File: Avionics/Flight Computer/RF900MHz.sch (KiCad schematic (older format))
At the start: 25 parts, among them J1 CONN_COAXIAL, U1 CC1310F128RGZR, U2 CC1190RGVR

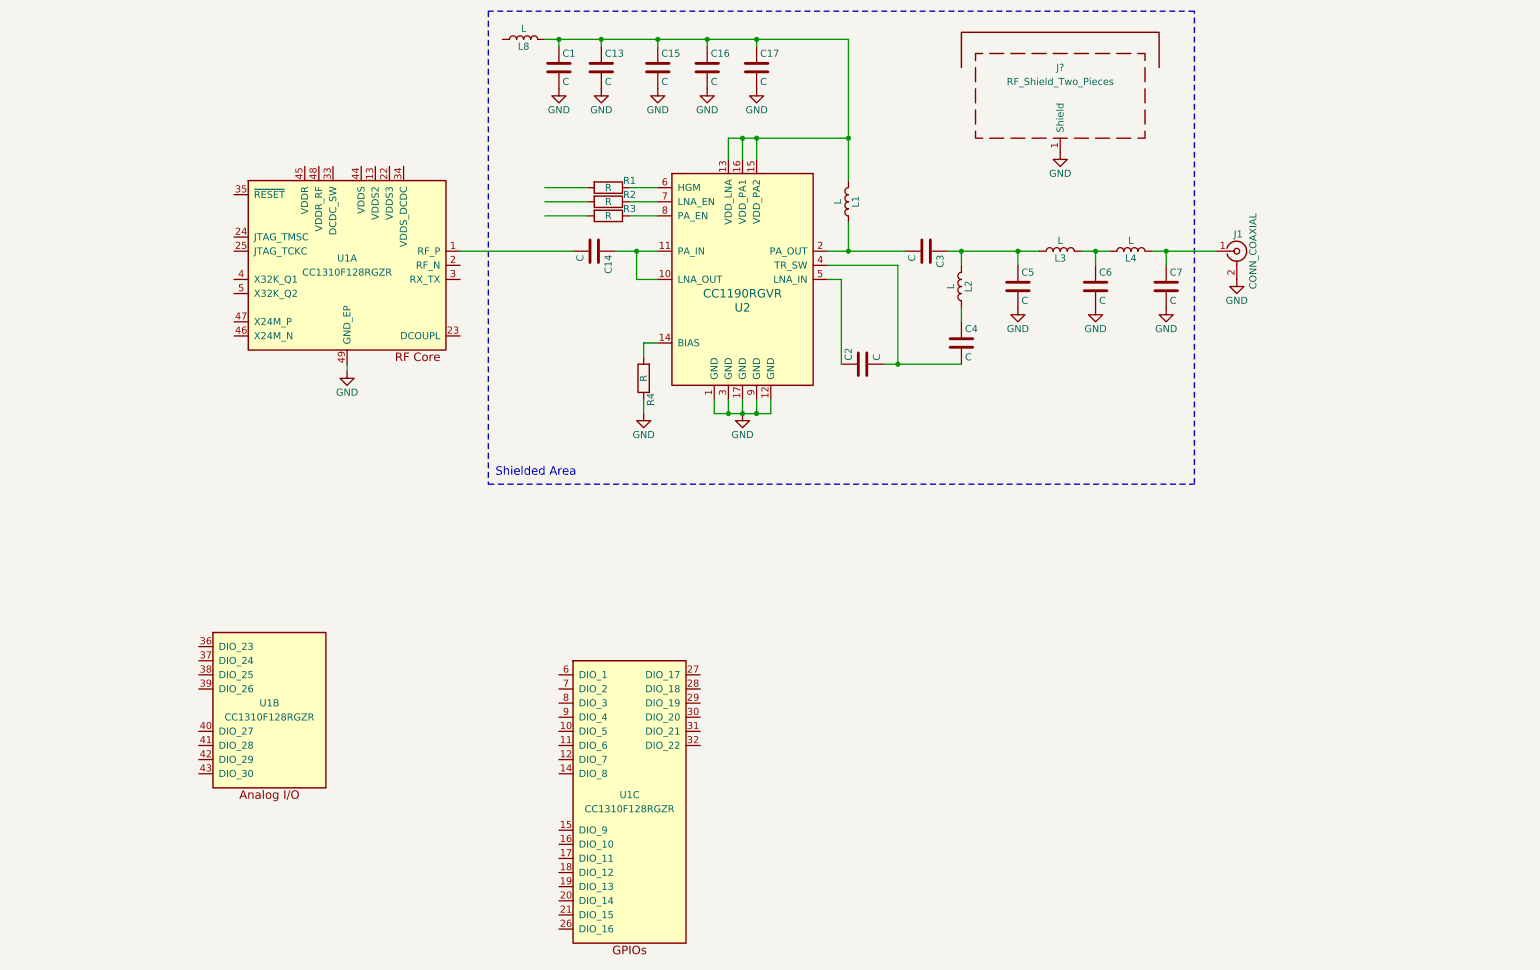
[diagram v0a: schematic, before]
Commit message: Added more RF passives and placement of RF front ends
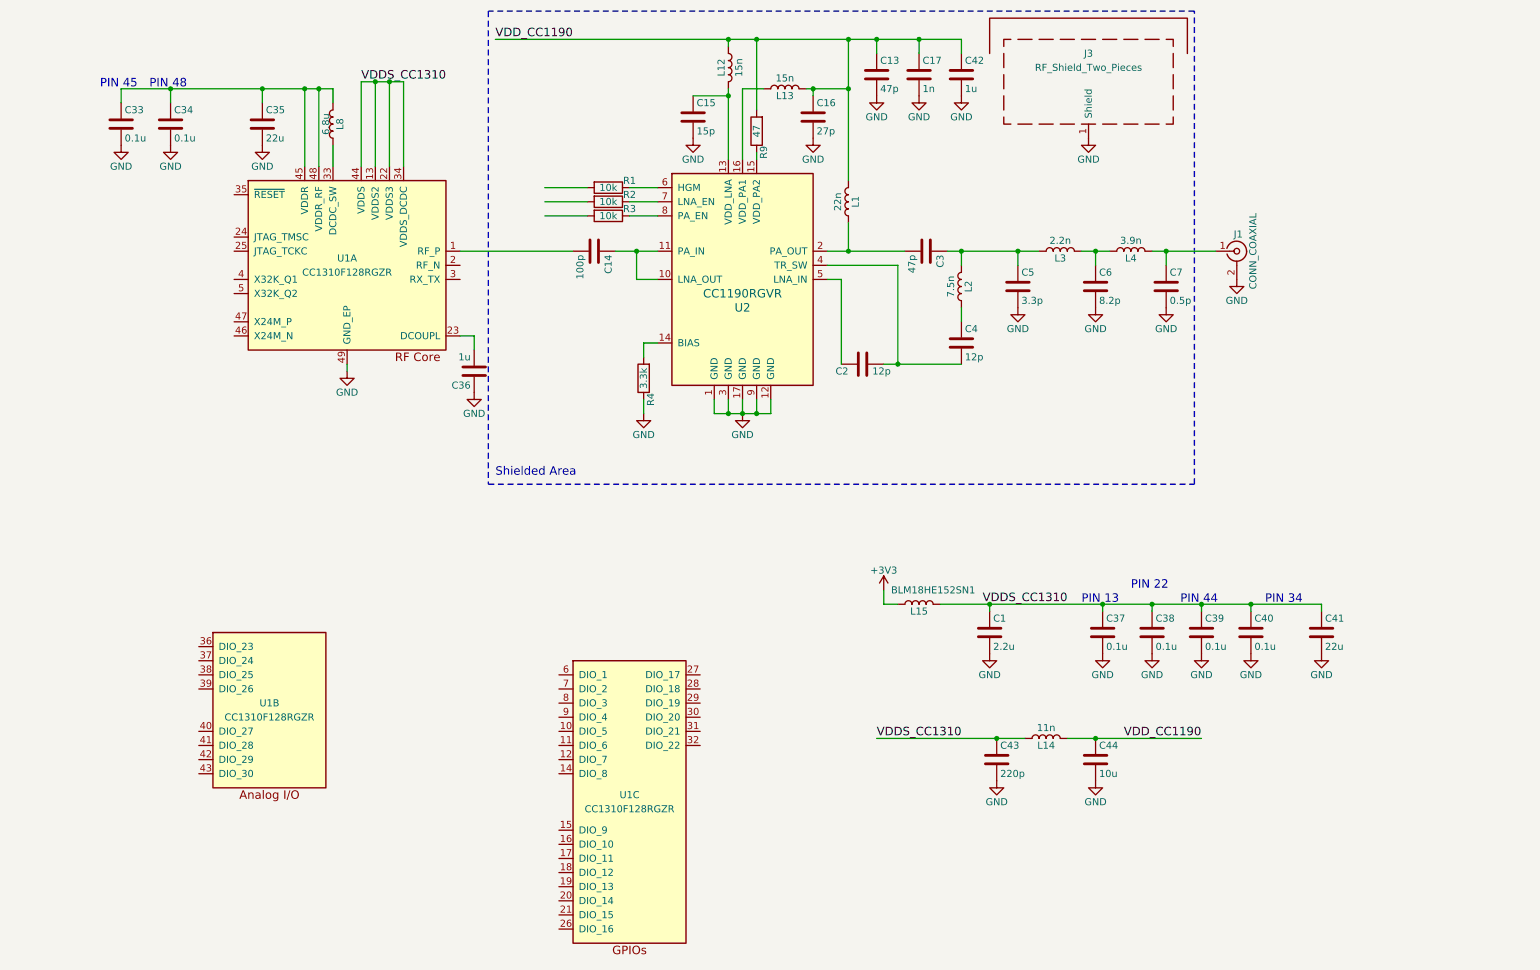
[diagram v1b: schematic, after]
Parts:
- added C33, C34, C37, C38, C39, C40: 0.1u, Capacitors_SMD:C_0402, symbol C
- added C35, C41: 22u, Capacitors_SMD:C_0603, symbol C
- added C36, C42: 1u, Capacitors_SMD:C_0402, symbol C
- added C43: 220p, Capacitors_SMD:C_0402, symbol C
- added C44: 10u, Capacitors_SMD:C_0603, symbol C
- added L12, L13: 15n, Inductors_SMD:L_0402, symbol L
- added L14: 11n, Inductors_SMD:L_0603, symbol L
- added L8: 6.8u, Inductors_SMD:L_0402, symbol L
- added R9: 47, Resistors_SMD:R_0402, symbol R
- C1: value C -> 2.2u
- C13, C3: value C -> 47p
- C14: value C -> 100p
- C15: value C -> 15p
- C16: value C -> 27p
- C17: value C -> 1n
- C2, C4: value C -> 12p
- C5: value C -> 3.3p
- C6: value C -> 8.2p
- C7: value C -> 0.5p
- L1: value L -> 22n; footprint Inductors_SMD:L_0402 -> Inductors_SMD:L_0603
- L15: renamed from L8; value L -> BLM18HE152SN1
- L2: value L -> 7.5n
- L3: value L -> 2.2n
- L4: value L -> 3.9n
- R1, R2, R3: value R -> 10k; footprint (none) -> Resistors_SMD:R_0402
- R4: value R -> 3.3k; footprint (none) -> Resistors_SMD:R_0402
- gave numbers to parts that had none: 1
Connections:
- net labels added: +3V3, VDDS_CC1310, VDD_CC1190
- wire segments 46 -> 75
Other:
- note added: "PIN 13"
- note added: "PIN 22"
- note added: "PIN 34"
- note added: "PIN 44"
- note added: "PIN 45"
- note added: "PIN 48"
- moved on the sheet: C1, C13, J3, L15

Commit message: Lots of power tree and layout work
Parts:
- J3: value RF_Shield_Two_Pieces -> BMI-S-202-F
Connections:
- net labels added: +3.3V
- net labels removed: +3V3
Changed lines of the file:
@@
 LIBS:graphic
 LIBS:power
+LIBS:interface
+LIBS:linear
+LIBS:74xgxx
+LIBS:74xx
+LIBS:ac-dc
+LIBS:actel
+LIBS:adc-dac
+LIBS:allegro
+LIBS:Altera
+LIBS:analog_devices
+LIBS:analog_switches
+LIBS:Power_Management
+LIBS:powerint
 LIBS:Flight Computer-cache
-EELAYER 25 0
+EELAYER 26 0
 EELAYER END
 $Descr A4 11693 8268
@@
 $EndComp
 $Comp
-L GND #PWR28
+L GND #PWR05
 U 1 1 58AA1A95
 P 9000 2500
-F 0 "#PWR28" H 9000 2250 50  0001 C CNN
+F 0 "#PWR05" H 9000 2250 50  0001 C CNN
 F 1 "GND" H 9000 2350 50  0000 C CNN
 F 2 "" H 9000 2500 50  0001 C CNN
@@
 $EndComp
 $Comp
-L GND #PWR26
+L GND #PWR06
 U 1 1 58AA3683
 P 8500 2700
-F 0 "#PWR26" H 8500 2450 50  0001 C CNN
+F 0 "#PWR06" H 8500 2450 50  0001 C CNN
 F 1 "GND" H 8500 2550 50  0000 C CNN
 F 2 "" H 8500 2700 50  0001 C CNN
@@
 $EndComp
 $Comp
-L GND #PWR22
+L GND #PWR07
 U 1 1 58AA36BB
 P 8000 2700
-F 0 "#PWR22" H 8000 2450 50  0001 C CNN
+F 0 "#PWR07" H 8000 2450 50  0001 C CNN
 F 1 "GND" H 8000 2550 50  0000 C CNN
 F 2 "" H 8000 2700 50  0001 C CNN
@@
 $EndComp
 $Comp
-L GND #PWR20
+L GND #PWR08
 U 1 1 58AA36F3
 P 7450 2700
-F 0 "#PWR20" H 7450 2450 50  0001 C CNN
+F 0 "#PWR08" H 7450 2450 50  0001 C CNN
 F 1 "GND" H 7450 2550 50  0000 C CNN
 F 2 "" H 7450 2700 50  0001 C CNN
@@
 $EndComp
 $Comp
-L GND #PWR12
+L GND #PWR09
 U 1 1 58AA409E
 P 5500 3450
-F 0 "#PWR12" H 5500 3200 50  0001 C CNN
+F 0 "#PWR09" H 5500 3200 50  0001 C CNN
 F 1 "GND" H 5500 3300 50  0000 C CNN
 F 2 "" H 5500 3450 50  0001 C CNN
@@
 $EndComp
 $Comp
-L GND #PWR8
+L GND #PWR010
 U 1 1 58AA431F
 P 2700 3150
-F 0 "#PWR8" H 2700 2900 50  0001 C CNN
+F 0 "#PWR010" H 2700 2900 50  0001 C CNN
 F 1 "GND" H 2700 3000 50  0000 C CNN
 F 2 "" H 2700 3150 50  0001 C CNN
@@
 $EndComp
 $Comp
-L GND #PWR18
+L GND #PWR011
 U 1 1 58AABD29
 P 7250 5150
-F 0 "#PWR18" H 7250 4900 50  0001 C CNN
+F 0 "#PWR011" H 7250 4900 50  0001 C CNN
 F 1 "GND" H 7250 5000 50  0000 C CNN
 F 2 "" H 7250 5150 50  0001 C CNN
@@
 $EndComp
 $Comp
-L GND #PWR11
+L GND #PWR012
 U 1 1 58AAF7AF
 P 5150 1500
-F 0 "#PWR11" H 5150 1250 50  0001 C CNN
+F 0 "#PWR012" H 5150 1250 50  0001 C CNN
 F 1 "GND" H 5150 1350 50  0000 C CNN
 F 2 "" H 5150 1500 50  0001 C CNN
@@
 $EndComp
 $Comp
-L GND #PWR10
+L GND #PWR013
 U 1 1 58AB0BB7
 P 4800 3450
-F 0 "#PWR10" H 4800 3200 50  0001 C CNN
+F 0 "#PWR013" H 4800 3200 50  0001 C CNN
 F 1 "GND" H 4800 3300 50  0000 C CNN
 F 2 "" H 4800 3450 50  0001 C CNN
@@
 $EndComp
 $Comp
-L GND #PWR21
+L GND #PWR014
 U 1 1 58AB2D32
 P 7950 1500
-F 0 "#PWR21" H 7950 1250 50  0001 C CNN
+F 0 "#PWR014" H 7950 1250 50  0001 C CNN
 F 1 "GND" H 7950 1350 50  0000 C CNN
 F 2 "" H 7950 1500 50  0001 C CNN
@@
 P 7950 1100
 F 0 "J3" H 7950 1300 50  0000 C CNN
-F 1 "RF_Shield_Two_Pieces" H 7950 1200 50  0000 C CNN
+F 1 "BMI-S-202-F" H 7950 1200 50  0000 C CNN
 F 2 "Shielding_Cabinets:Laird_Technologies_BMI-S-202-F_16.50x16.50mm" H 7950 1000 50  0001 C CNN
 F 3 "" H 7950 1000 50  0001 C CNN
@@
 Text Label 7200 4800 0    60   ~ 0
 VDDS_CC1310
-$Comp
-L +3V3 #PWR15
-U 1 1 58AE2EAF
-P 6500 4700
-F 0 "#PWR15" H 6500 4550 50  0001 C CNN
-F 1 "+3V3" H 6500 4840 50  0000 C CNN
-F 2 "" H 6500 4700 50  0001 C CNN
-F 3 "" H 6500 4700 50  0001 C CNN
-	1    6500 4700
-	1    0    0    -1
-$EndComp
 $Comp
 L C C36
@@
 $EndComp
 $Comp
-L GND #PWR9
+L GND #PWR015
 U 1 1 58AE74D7
 P 3600 3300
-F 0 "#PWR9" H 3600 3050 50  0001 C CNN
+F 0 "#PWR015" H 3600 3050 50  0001 C CNN
 F 1 "GND" H 3600 3150 50  0000 C CNN
 F 2 "" H 3600 3300 50  0001 C CNN
@@
 $EndComp
 $Comp
-L GND #PWR24
+L GND #PWR016
 U 1 1 58AF2937
 P 8050 5150
-F 0 "#PWR24" H 8050 4900 50  0001 C CNN
+F 0 "#PWR016" H 8050 4900 50  0001 C CNN
 F 1 "GND" H 8050 5000 50  0000 C CNN
 F 2 "" H 8050 5150 50  0001 C CNN
@@
 $EndComp
 $Comp
-L GND #PWR25
+L GND #PWR017
 U 1 1 58AF2A67
 P 8400 5150
-F 0 "#PWR25" H 8400 4900 50  0001 C CNN
+F 0 "#PWR017" H 8400 4900 50  0001 C CNN
 F 1 "GND" H 8400 5000 50  0000 C CNN
 F 2 "" H 8400 5150 50  0001 C CNN
@@
 $EndComp
 $Comp
-L GND #PWR27
+L GND #PWR018
 U 1 1 58AF2BB0
 P 8750 5150
-F 0 "#PWR27" H 8750 4900 50  0001 C CNN
+F 0 "#PWR018" H 8750 4900 50  0001 C CNN
 F 1 "GND" H 8750 5000 50  0000 C CNN
 F 2 "" H 8750 5150 50  0001 C CNN
@@
 $EndComp
 $Comp
-L GND #PWR29
+L GND #PWR019
 U 1 1 58AF2C21
 P 9100 5150
-F 0 "#PWR29" H 9100 4900 50  0001 C CNN
+F 0 "#PWR019" H 9100 4900 50  0001 C CNN
 F 1 "GND" H 9100 5000 50  0000 C CNN
 F 2 "" H 9100 5150 50  0001 C CNN
@@
 	9600 4800 9600 4850
 $Comp
-L GND #PWR30
+L GND #PWR020
 U 1 1 58AF39C7
 P 9600 5150
-F 0 "#PWR30" H 9600 4900 50  0001 C CNN
+F 0 "#PWR020" H 9600 4900 50  0001 C CNN
 F 1 "GND" H 9600 5000 50  0000 C CNN
 F 2 "" H 9600 5150 50  0001 C CNN
@@
 Connection ~ 2500 1150
 $Comp
-L GND #PWR7
+L GND #PWR021
 U 1 1 58AF55B9
 P 2100 1550
-F 0 "#PWR7" H 2100 1300 50  0001 C CNN
+F 0 "#PWR021" H 2100 1300 50  0001 C CNN
 F 1 "GND" H 2100 1400 50  0000 C CNN
 F 2 "" H 2100 1550 50  0001 C CNN
@@
 Connection ~ 1450 1150
 $Comp
-L GND #PWR6
+L GND #PWR022
 U 1 1 58AF6EFE
 P 1450 1550
-F 0 "#PWR6" H 1450 1300 50  0001 C CNN
+F 0 "#PWR022" H 1450 1300 50  0001 C CNN
 F 1 "GND" H 1450 1400 50  0000 C CNN
 F 2 "" H 1450 1550 50  0001 C CNN
@@
 $EndComp
 $Comp
-L GND #PWR5
+L GND #PWR023
 U 1 1 58AF6F78
 P 1100 1550
-F 0 "#PWR5" H 1100 1300 50  0001 C CNN
+F 0 "#PWR023" H 1100 1300 50  0001 C CNN
 F 1 "GND" H 1100 1400 50  0000 C CNN
 F 2 "" H 1100 1550 50  0001 C CNN
@@
 $EndComp
 $Comp
-L GND #PWR14
+L GND #PWR024
 U 1 1 58AF9836
 P 6450 1200
-F 0 "#PWR14" H 6450 950 50  0001 C CNN
+F 0 "#PWR024" H 6450 950 50  0001 C CNN
 F 1 "GND" H 6450 1050 50  0000 C CNN
 F 2 "" H 6450 1200 50  0001 C CNN
@@
 $EndComp
 $Comp
-L GND #PWR16
+L GND #PWR025
 U 1 1 58AF99F1
 P 6750 1200
-F 0 "#PWR16" H 6750 950 50  0001 C CNN
+F 0 "#PWR025" H 6750 950 50  0001 C CNN
 F 1 "GND" H 6750 1050 50  0000 C CNN
 F 2 "" H 6750 1200 50  0001 C CNN
@@
 $EndComp
 $Comp
-L GND #PWR17
+L GND #PWR026
 U 1 1 58AF9A68
 P 7050 1200
-F 0 "#PWR17" H 7050 950 50  0001 C CNN
+F 0 "#PWR026" H 7050 950 50  0001 C CNN
 F 1 "GND" H 7050 1050 50  0000 C CNN
 F 2 "" H 7050 1200 50  0001 C CNN
@@
 Connection ~ 6000 1150
 $Comp
-L GND #PWR13
+L GND #PWR027
 U 1 1 58AFAEF6
 P 6000 1500
-F 0 "#PWR13" H 6000 1250 50  0001 C CNN
+F 0 "#PWR027" H 6000 1250 50  0001 C CNN
 F 1 "GND" H 6000 1350 50  0000 C CNN
 F 2 "" H 6000 1500 50  0001 C CNN
@@
 $EndComp
 $Comp
-L GND #PWR19
+L GND #PWR028
 U 1 1 58AFDA75
 P 7300 6050
-F 0 "#PWR19" H 7300 5800 50  0001 C CNN
+F 0 "#PWR028" H 7300 5800 50  0001 C CNN
 F 1 "GND" H 7300 5900 50  0000 C CNN
 F 2 "" H 7300 6050 50  0001 C CNN
@@
 $EndComp
 $Comp
-L GND #PWR23
+L GND #PWR029
 U 1 1 58AFDB01
 P 8000 6050
-F 0 "#PWR23" H 8000 5800 50  0001 C CNN
+F 0 "#PWR029" H 8000 5800 50  0001 C CNN
 F 1 "GND" H 8000 5900 50  0000 C CNN
 F 2 "" H 8000 6050 50  0001 C CNN
@@
 Connection ~ 7300 5750
 Connection ~ 8000 5750
+$Comp
+L +3.3V #PWR030
+U 1 1 58ABA1EC
+P 6500 4700
+F 0 "#PWR030" H 6550 4750 50  0001 C CNN
+F 1 "+3.3V" H 6515 4873 50  0000 C CNN
+F 2 "" H -150 250 50  0001 C CNN
+F 3 "" H -150 250 50  0001 C CNN
+	1    6500 4700
+	1    0    0    -1
+$EndComp
 $EndSCHEMATC
